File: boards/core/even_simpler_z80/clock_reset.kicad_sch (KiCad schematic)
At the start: 10 parts, among them J2 EXT_CLK, J3 CPU_CLK_SEL, J4 BUS_CLK_SEL, U2 74LS04, U6 74LS08, X1 INT_CLK

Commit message: * Working on new powerdistribution method.
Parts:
- removed unit 4 of U2
- removed unit 7 of U2
- D1: value D -> 1N4148
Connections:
- no-connect marks 7 -> 5

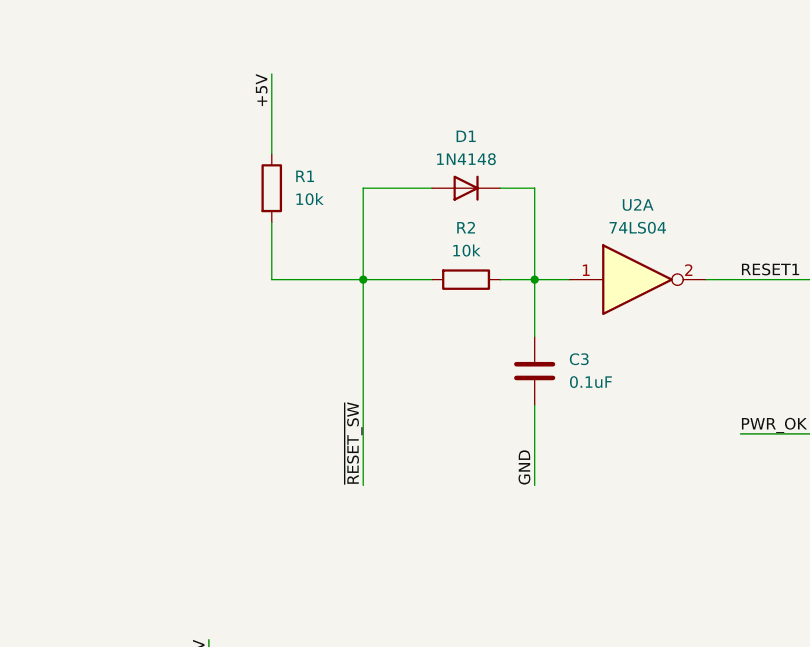
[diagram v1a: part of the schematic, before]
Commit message: Added expansion connector C and designed some new boards around it.
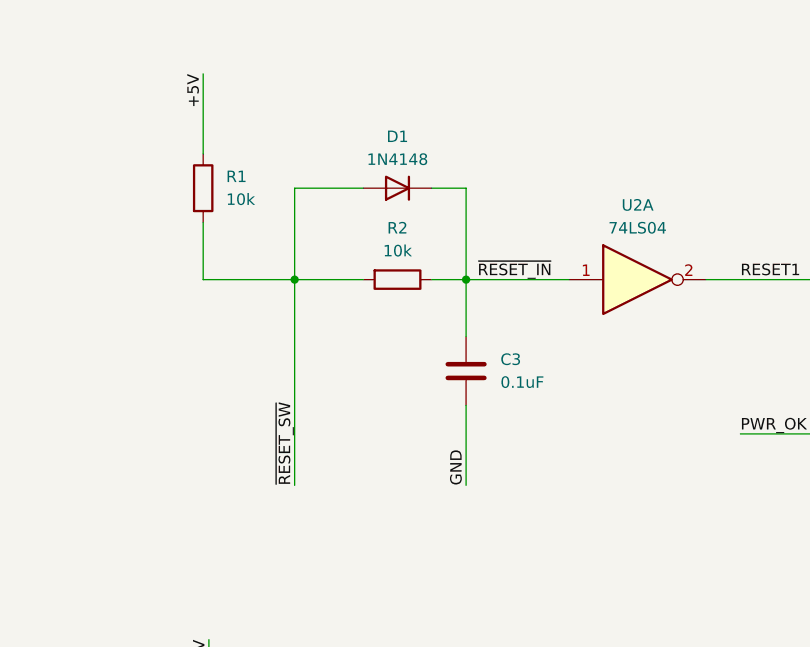
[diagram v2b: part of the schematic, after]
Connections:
- net ~{RESET_IN}: now reaches C3.1, D1.1 (K), R2.1, U2.1
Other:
- moved on the sheet: C3, D1, R1, R2
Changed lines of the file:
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@@
     (rev "1.4")
   )
-  (junction (at 165.1 43.815) (diameter 0) (color 0 0 0 0)
-  )
-  (junction (at 184.15 43.815) (diameter 0) (color 0 0 0 0)
+  (junction (at 157.48 43.815) (diameter 0) (color 0 0 0 0)
+  )
+  (junction (at 176.53 43.815) (diameter 0) (color 0 0 0 0)
   )
   (no_connect (at 171.45 169.545))
@@
     (stroke (width 0) (type default))
   )
-  (wire (pts (xy 184.15 33.655) (xy 184.15 43.815))
+  (wire (pts (xy 176.53 33.655) (xy 176.53 43.815))
     (stroke (width 0) (type default))
   )
@@
     (stroke (width 0) (type default))
   )
-  (wire (pts (xy 180.34 33.655) (xy 184.15 33.655))
+  (wire (pts (xy 172.72 33.655) (xy 176.53 33.655))
     (stroke (width 0) (type default))
   )
@@
     (stroke (width 0) (type default))
   )
-  (wire (pts (xy 165.1 43.815) (xy 154.94 43.815))
+  (wire (pts (xy 157.48 43.815) (xy 147.32 43.815))
     (stroke (width 0) (type default))
   )
@@
     (stroke (width 0) (type default))
   )
-  (wire (pts (xy 184.15 43.815) (xy 187.96 43.815))
-    (stroke (width 0) (type default))
-  )
-  (wire (pts (xy 154.94 43.815) (xy 154.94 37.465))
+  (wire (pts (xy 176.53 43.815) (xy 187.96 43.815))
+    (stroke (width 0) (type default))
+  )
+  (wire (pts (xy 147.32 43.815) (xy 147.32 37.465))
     (stroke (width 0) (type default))
   )
@@
     (stroke (width 0) (type default))
   )
-  (wire (pts (xy 165.1 33.655) (xy 165.1 43.815))
+  (wire (pts (xy 157.48 33.655) (xy 157.48 43.815))
     (stroke (width 0) (type default))
   )
@@
     (stroke (width 0) (type default))
   )
-  (wire (pts (xy 184.15 43.815) (xy 184.15 50.165))
+  (wire (pts (xy 176.53 43.815) (xy 176.53 50.165))
     (stroke (width 0) (type default))
   )
@@
     (stroke (width 0) (type default))
   )
-  (wire (pts (xy 172.72 33.655) (xy 165.1 33.655))
+  (wire (pts (xy 165.1 33.655) (xy 157.48 33.655))
     (stroke (width 0) (type default))
   )
@@
     (stroke (width 0) (type default))
   )
-  (wire (pts (xy 180.34 43.815) (xy 184.15 43.815))
+  (wire (pts (xy 172.72 43.815) (xy 176.53 43.815))
     (stroke (width 0) (type default))
   )
@@
     (stroke (width 0) (type default))
   )
-  (wire (pts (xy 165.1 43.815) (xy 165.1 66.675))
+  (wire (pts (xy 157.48 43.815) (xy 157.48 66.675))
     (stroke (width 0) (type default))
   )
@@
     (stroke (width 0) (type default))
   )
-  (wire (pts (xy 184.15 66.675) (xy 184.15 57.785))
+  (wire (pts (xy 176.53 66.675) (xy 176.53 57.785))
     (stroke (width 0) (type default))
   )
@@
     (stroke (width 0) (type default))
   )
-  (wire (pts (xy 172.72 43.815) (xy 165.1 43.815))
-    (stroke (width 0) (type default))
-  )
-  (wire (pts (xy 154.94 20.955) (xy 154.94 29.845))
+  (wire (pts (xy 165.1 43.815) (xy 157.48 43.815))
+    (stroke (width 0) (type default))
+  )
+  (wire (pts (xy 147.32 20.955) (xy 147.32 29.845))
     (stroke (width 0) (type default))
   )
@@
     (effects (font (size 1.27 1.27)) (justify left bottom))
   )
-  (label "~{RESET_SW}" (at 165.1 66.675 90) (fields_autoplaced)
+  (label "~{RESET_SW}" (at 157.48 66.675 90) (fields_autoplaced)
     (effects (font (size 1.27 1.27)) (justify left bottom))
   )
@@
     (effects (font (size 1.27 1.27)) (justify left bottom))
   )
-  (label "+5V" (at 154.94 20.955 270) (fields_autoplaced)
+  (label "+5V" (at 147.32 20.955 270) (fields_autoplaced)
     (effects (font (size 1.27 1.27)) (justify right bottom))
   )
@@
     (effects (font (size 1.27 1.27)) (justify left bottom))
   )
-  (label "GND" (at 184.15 66.675 90) (fields_autoplaced)
+  (label "GND" (at 176.53 66.675 90) (fields_autoplaced)
     (effects (font (size 1.27 1.27)) (justify left bottom))
   )
@@
   (label "~{RESET_SW}" (at 36.195 24.13 180) (fields_autoplaced)
     (effects (font (size 1.27 1.27)) (justify right bottom))
+  )
+  (label "~{RESET_IN}" (at 177.8 43.815 0) (fields_autoplaced)
+    (effects (font (size 1.27 1.27)) (justify left bottom))
   )
   (label "PWR_OK" (at 36.195 27.305 180) (fields_autoplaced)
@@
     )
   )
-  (symbol (lib_id "Device:R") (at 176.53 43.815 270) (unit 1)
-    (in_bom yes) (on_board yes) (dnp no) (fields_autoplaced)
-    (property "Reference" "R2" (at 176.53 38.1 90)
-      (effects (font (size 1.27 1.27)))
-    )
-    (property "Value" "10k" (at 176.53 40.64 90)
-      (effects (font (size 1.27 1.27)))
-    )
-    (property "Footprint" "Resistor_THT:R_Axial_DIN0204_L3.6mm_D1.6mm_P7.62mm_Horizontal" (at 176.53 42.037 90)
-      (effects (font (size 1.27 1.27)) hide)
-    )
-    (property "Datasheet" "~" (at 176.53 43.815 0)
+  (symbol (lib_id "Device:R") (at 168.91 43.815 270) (unit 1)
+    (in_bom yes) (on_board yes) (dnp no) (fields_autoplaced)
+    (property "Reference" "R2" (at 168.91 38.1 90)
+      (effects (font (size 1.27 1.27)))
+    )
+    (property "Value" "10k" (at 168.91 40.64 90)
+      (effects (font (size 1.27 1.27)))
+    )
+    (property "Footprint" "Resistor_THT:R_Axial_DIN0204_L3.6mm_D1.6mm_P7.62mm_Horizontal" (at 168.91 42.037 90)
+      (effects (font (size 1.27 1.27)) hide)
+    )
+    (property "Datasheet" "~" (at 168.91 43.815 0)
       (effects (font (size 1.27 1.27)) hide)
     )
@@
     )
   )
-  (symbol (lib_id "Device:C") (at 184.15 53.975 0) (unit 1)
-    (in_bom yes) (on_board yes) (dnp no) (fields_autoplaced)
-    (property "Reference" "C3" (at 187.96 52.705 0)
+  (symbol (lib_id "Device:C") (at 176.53 53.975 0) (unit 1)
+    (in_bom yes) (on_board yes) (dnp no) (fields_autoplaced)
+    (property "Reference" "C3" (at 180.34 52.705 0)
       (effects (font (size 1.27 1.27)) (justify left))
     )
-    (property "Value" "0.1uF" (at 187.96 55.245 0)
+    (property "Value" "0.1uF" (at 180.34 55.245 0)
       (effects (font (size 1.27 1.27)) (justify left))
     )
-    (property "Footprint" "Capacitor_THT:C_Disc_D5.0mm_W2.5mm_P2.50mm" (at 185.1152 57.785 0)
-      (effects (font (size 1.27 1.27)) hide)
-    )
-    (property "Datasheet" "~" (at 184.15 53.975 0)
+    (property "Footprint" "Capacitor_THT:C_Disc_D5.0mm_W2.5mm_P2.50mm" (at 177.4952 57.785 0)
+      (effects (font (size 1.27 1.27)) hide)
+    )
+    (property "Datasheet" "~" (at 176.53 53.975 0)
       (effects (font (size 1.27 1.27)) hide)
     )
@@
     )
   )
-  (symbol (lib_id "Device:D") (at 176.53 33.655 180) (unit 1)
-    (in_bom yes) (on_board yes) (dnp no) (fields_autoplaced)
-    (property "Reference" "D1" (at 176.53 27.94 0)
-      (effects (font (size 1.27 1.27)))
-    )
-    (property "Value" "1N4148" (at 176.53 30.48 0)
-      (effects (font (size 1.27 1.27)))
-    )
-    (property "Footprint" "Diode_THT:D_A-405_P7.62mm_Horizontal" (at 176.53 33.655 0)
-      (effects (font (size 1.27 1.27)) hide)
-    )
-    (property "Datasheet" "~" (at 176.53 33.655 0)
-      (effects (font (size 1.27 1.27)) hide)
-    )
-    (property "Sim.Device" "D" (at 176.53 33.655 0)
-      (effects (font (size 1.27 1.27)) hide)
-    )
-    (property "Sim.Pins" "1=K 2=A" (at 176.53 33.655 0)
+  (symbol (lib_id "Device:D") (at 168.91 33.655 180) (unit 1)
+    (in_bom yes) (on_board yes) (dnp no) (fields_autoplaced)
+    (property "Reference" "D1" (at 168.91 27.94 0)
+      (effects (font (size 1.27 1.27)))
+    )
+    (property "Value" "1N4148" (at 168.91 30.48 0)
+      (effects (font (size 1.27 1.27)))
+    )
+    (property "Footprint" "Diode_THT:D_A-405_P7.62mm_Horizontal" (at 168.91 33.655 0)
+      (effects (font (size 1.27 1.27)) hide)
+    )
+    (property "Datasheet" "~" (at 168.91 33.655 0)
+      (effects (font (size 1.27 1.27)) hide)
+    )
+    (property "Sim.Device" "D" (at 168.91 33.655 0)
+      (effects (font (size 1.27 1.27)) hide)
+    )
+    (property "Sim.Pins" "1=K 2=A" (at 168.91 33.655 0)
       (effects (font (size 1.27 1.27)) hide)
     )
@@
     )
   )
-  (symbol (lib_id "Device:R") (at 154.94 33.655 0) (unit 1)
-    (in_bom yes) (on_board yes) (dnp no) (fields_autoplaced)
-    (property "Reference" "R1" (at 157.48 32.385 0)
+  (symbol (lib_id "Device:R") (at 147.32 33.655 0) (unit 1)
+    (in_bom yes) (on_board yes) (dnp no) (fields_autoplaced)
+    (property "Reference" "R1" (at 149.86 32.385 0)
       (effects (font (size 1.27 1.27)) (justify left))
     )
-    (property "Value" "10k" (at 157.48 34.925 0)
+    (property "Value" "10k" (at 149.86 34.925 0)
       (effects (font (size 1.27 1.27)) (justify left))
     )
-    (property "Footprint" "Resistor_THT:R_Axial_DIN0204_L3.6mm_D1.6mm_P7.62mm_Horizontal" (at 153.162 33.655 90)
-      (effects (font (size 1.27 1.27)) hide)
-    )
-    (property "Datasheet" "~" (at 154.94 33.655 0)
-      (effects (font (size 1.27 1.27)) hide)
-    )
+    (property "Footprint" "Resistor_THT:R_Axial_DIN0204_L3.6mm_D1.6mm_P7.62mm_Horizontal" (at 145.542 33.655 90)
+      (effects (font (size 1.27 1.27)) hide)
+    )
+    (property "Datasheet" "~" (at 147.32 33.655 0)
+      (effects (font (size 1.27 1.27)) hide)
+    )
